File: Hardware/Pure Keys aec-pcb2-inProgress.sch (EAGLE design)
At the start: 56 parts, among them IC1 MCP6004P, IC5 MCP6004P, Q2 20MHz, T1 2N3904, U2 LM4040, U3 328P

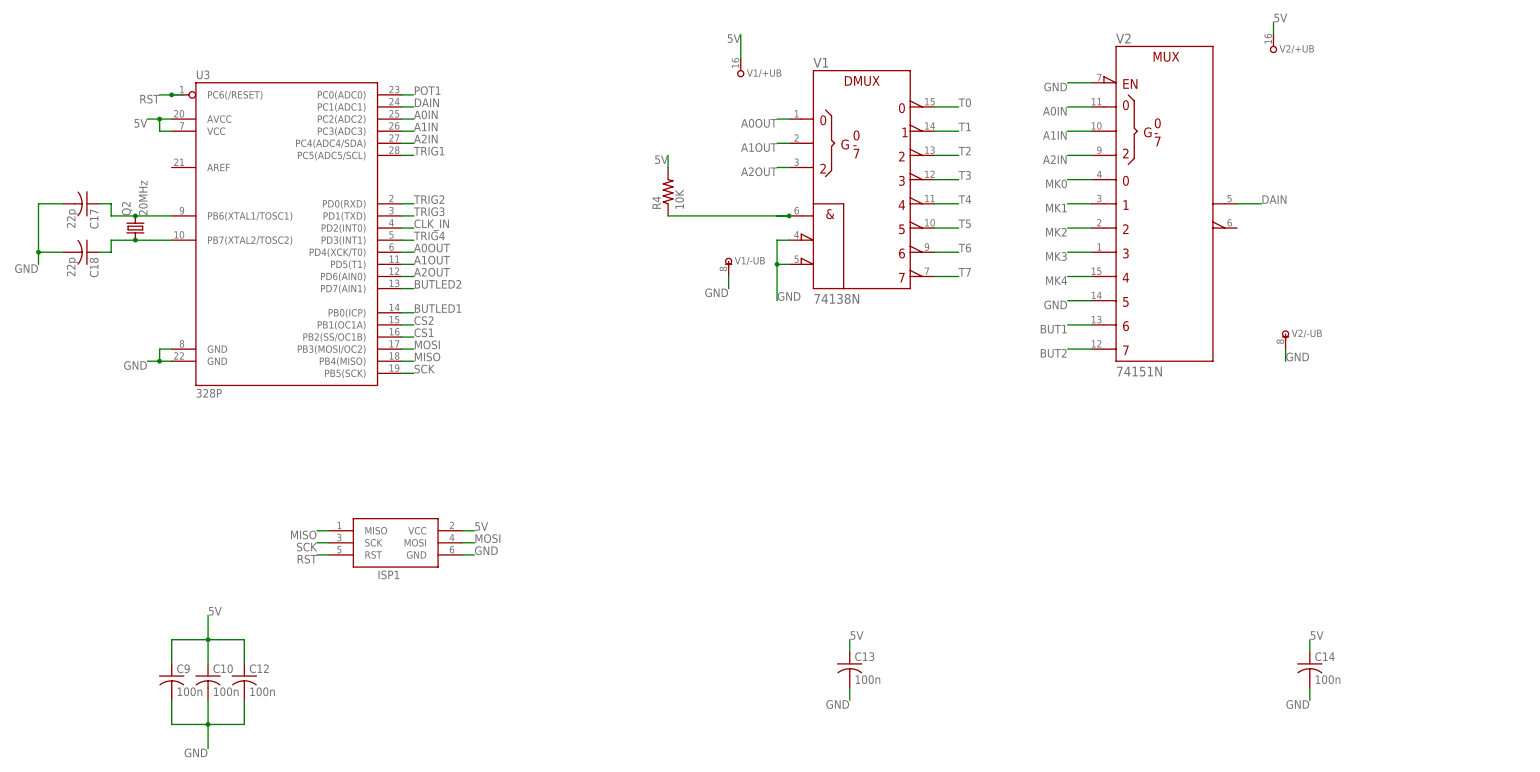
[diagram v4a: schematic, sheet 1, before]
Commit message: Updated routing on in-progress board to make room for 1K pull downs
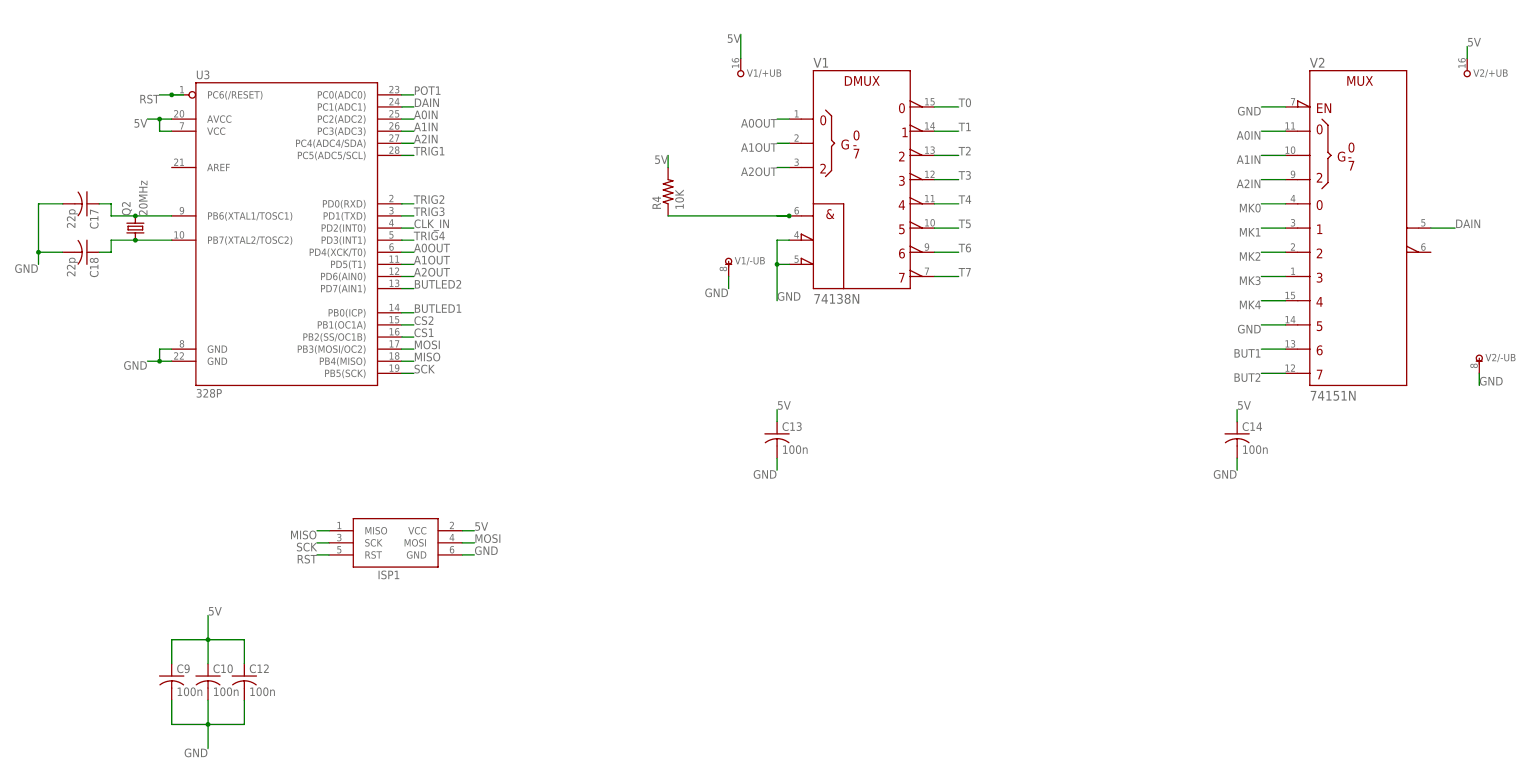
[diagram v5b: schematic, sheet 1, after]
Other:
- moved on the sheet: C13, C14, V2, V2/+UB, V2/-UB
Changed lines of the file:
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@@
 <instance part="C10" gate="G$1" x="25.4" y="43.18"/>
 <instance part="C12" gate="G$1" x="33.02" y="43.18"/>
-<instance part="C13" gate="G$1" x="160.02" y="45.72"/>
-<instance part="C14" gate="G$1" x="256.54" y="45.72"/>
+<instance part="C13" gate="G$1" x="144.78" y="93.98"/>
+<instance part="C14" gate="G$1" x="241.3" y="93.98"/>
 <instance part="V1" gate="1" x="162.56" y="147.32"/>
-<instance part="V2" gate="1" x="226.06" y="142.24"/>
+<instance part="V2" gate="1" x="266.7" y="137.16"/>
 <instance part="U3" gate="G$1" x="40.64" y="139.7"/>
 <instance part="Q2" gate="G$1" x="10.16" y="137.16" rot="R90"/>
@@
 <instance part="V1" gate="/+UB" x="137.16" y="170.18"/>
 <instance part="V1" gate="/-UB" x="134.62" y="129.54"/>
-<instance part="V2" gate="/+UB" x="248.92" y="175.26"/>
-<instance part="V2" gate="/-UB" x="251.46" y="114.3"/>
+<instance part="V2" gate="/+UB" x="289.56" y="170.18"/>
+<instance part="V2" gate="/-UB" x="292.1" y="109.22"/>
 <instance part="R4" gate="G$1" x="121.92" y="144.78" rot="R90"/>
 </instances>
@@
 <segment>
 <pinref part="C14" gate="G$1" pin="2"/>
-<wire x1="256.54" y1="40.64" x2="256.54" y2="38.1" width="0.1524" layer="91"/>
-<label x="256.54" y="38.1" size="1.778" layer="95" rot="R180"/>
+<wire x1="241.3" y1="88.9" x2="241.3" y2="86.36" width="0.1524" layer="91"/>
+<label x="241.3" y="86.36" size="1.778" layer="95" rot="R180"/>
 </segment>
 <segment>
 <pinref part="C13" gate="G$1" pin="2"/>
-<wire x1="160.02" y1="40.64" x2="160.02" y2="38.1" width="0.1524" layer="91"/>
-<label x="160.02" y="38.1" size="1.778" layer="95" rot="R180"/>
+<wire x1="144.78" y1="88.9" x2="144.78" y2="86.36" width="0.1524" layer="91"/>
+<label x="144.78" y="86.36" size="1.778" layer="95" rot="R180"/>
 </segment>
 <segment>
@@
 <segment>
 <pinref part="V2" gate="/-UB" pin="-UB"/>
-<wire x1="251.46" y1="111.76" x2="251.46" y2="109.22" width="0.1524" layer="91"/>
-<label x="251.46" y="109.22" size="1.778" layer="95"/>
+<wire x1="292.1" y1="106.68" x2="292.1" y2="104.14" width="0.1524" layer="91"/>
+<label x="292.1" y="104.14" size="1.778" layer="95"/>
 </segment>
 <segment>
 <pinref part="V2" gate="1" pin="D5"/>
-<wire x1="210.82" y1="121.92" x2="205.74" y2="121.92" width="0.1524" layer="91"/>
-<label x="205.74" y="121.92" size="1.778" layer="95" rot="R180"/>
+<wire x1="251.46" y1="116.84" x2="246.38" y2="116.84" width="0.1524" layer="91"/>
+<label x="246.38" y="116.84" size="1.778" layer="95" rot="R180"/>
 </segment>
 <segment>
 <pinref part="V2" gate="1" pin="!G"/>
-<wire x1="210.82" y1="167.64" x2="205.74" y2="167.64" width="0.1524" layer="91"/>
-<label x="205.74" y="167.64" size="1.778" layer="95" rot="R180"/>
+<wire x1="251.46" y1="162.56" x2="246.38" y2="162.56" width="0.1524" layer="91"/>
+<label x="246.38" y="162.56" size="1.778" layer="95" rot="R180"/>
 </segment>
 </net>
@@
 <segment>
 <pinref part="C13" gate="G$1" pin="1"/>
-<wire x1="160.02" y1="48.26" x2="160.02" y2="50.8" width="0.1524" layer="91"/>
-<label x="160.02" y="50.8" size="1.778" layer="95"/>
+<wire x1="144.78" y1="96.52" x2="144.78" y2="99.06" width="0.1524" layer="91"/>
+<label x="144.78" y="99.06" size="1.778" layer="95"/>
 </segment>
 <segment>
 <pinref part="C14" gate="G$1" pin="1"/>
-<wire x1="256.54" y1="48.26" x2="256.54" y2="50.8" width="0.1524" layer="91"/>
-<label x="256.54" y="50.8" size="1.778" layer="95"/>
+<wire x1="241.3" y1="96.52" x2="241.3" y2="99.06" width="0.1524" layer="91"/>
+<label x="241.3" y="99.06" size="1.778" layer="95"/>
 </segment>
 <segment>
@@
 <segment>
 <pinref part="V2" gate="/+UB" pin="+UB"/>
-<wire x1="248.92" y1="177.8" x2="248.92" y2="180.34" width="0.1524" layer="91"/>
-<label x="248.92" y="180.34" size="1.778" layer="95"/>
+<wire x1="289.56" y1="172.72" x2="289.56" y2="175.26" width="0.1524" layer="91"/>
+<label x="289.56" y="175.26" size="1.778" layer="95"/>
 </segment>
 <segment>
@@
 <segment>
 <pinref part="V2" gate="1" pin="D4"/>
-<wire x1="210.82" y1="127" x2="205.74" y2="127" width="0.1524" layer="91"/>
-<label x="205.74" y="127" size="1.778" layer="95" rot="R180"/>
+<wire x1="251.46" y1="121.92" x2="246.38" y2="121.92" width="0.1524" layer="91"/>
+<label x="246.38" y="121.92" size="1.778" layer="95" rot="R180"/>
 </segment>
 </net>
@@
 <segment>
 <pinref part="V2" gate="1" pin="D3"/>
-<wire x1="210.82" y1="132.08" x2="205.74" y2="132.08" width="0.1524" layer="91"/>
-<label x="205.74" y="132.08" size="1.778" layer="95" rot="R180"/>
+<wire x1="251.46" y1="127" x2="246.38" y2="127" width="0.1524" layer="91"/>
+<label x="246.38" y="127" size="1.778" layer="95" rot="R180"/>
 </segment>
 </net>
@@
 <segment>
 <pinref part="V2" gate="1" pin="D2"/>
-<wire x1="210.82" y1="137.16" x2="205.74" y2="137.16" width="0.1524" layer="91"/>
-<label x="205.74" y="137.16" size="1.778" layer="95" rot="R180"/>
+<wire x1="251.46" y1="132.08" x2="246.38" y2="132.08" width="0.1524" layer="91"/>
+<label x="246.38" y="132.08" size="1.778" layer="95" rot="R180"/>
 </segment>
 </net>
@@
 <segment>
 <pinref part="V2" gate="1" pin="Y"/>
-<wire x1="241.3" y1="142.24" x2="246.38" y2="142.24" width="0.1524" layer="91"/>
-<label x="246.38" y="142.24" size="1.778" layer="95"/>
+<wire x1="281.94" y1="137.16" x2="287.02" y2="137.16" width="0.1524" layer="91"/>
+<label x="287.02" y="137.16" size="1.778" layer="95"/>
 </segment>
 <segment>
@@
 <segment>
 <pinref part="V2" gate="1" pin="D6"/>
-<wire x1="210.82" y1="116.84" x2="205.74" y2="116.84" width="0.1524" layer="91"/>
-<label x="205.74" y="116.84" size="1.778" layer="95" rot="R180"/>
+<wire x1="251.46" y1="111.76" x2="246.38" y2="111.76" width="0.1524" layer="91"/>
+<label x="246.38" y="111.76" size="1.778" layer="95" rot="R180"/>
 </segment>
 </net>
@@
 <segment>
 <pinref part="V2" gate="1" pin="D7"/>
-<wire x1="210.82" y1="111.76" x2="205.74" y2="111.76" width="0.1524" layer="91"/>
-<label x="205.74" y="111.76" size="1.778" layer="95" rot="R180"/>
+<wire x1="251.46" y1="106.68" x2="246.38" y2="106.68" width="0.1524" layer="91"/>
+<label x="246.38" y="106.68" size="1.778" layer="95" rot="R180"/>
 </segment>
 </net>
@@
 <segment>
 <pinref part="V2" gate="1" pin="D1"/>
-<wire x1="210.82" y1="142.24" x2="205.74" y2="142.24" width="0.1524" layer="91"/>
-<label x="205.74" y="142.24" size="1.778" layer="95" rot="R180"/>
+<wire x1="251.46" y1="137.16" x2="246.38" y2="137.16" width="0.1524" layer="91"/>
+<label x="246.38" y="137.16" size="1.778" layer="95" rot="R180"/>
 </segment>
 </net>
@@
 <segment>
 <pinref part="V2" gate="1" pin="D0"/>
-<wire x1="210.82" y1="147.32" x2="205.74" y2="147.32" width="0.1524" layer="91"/>
-<label x="205.74" y="147.32" size="1.778" layer="95" rot="R180"/>
+<wire x1="251.46" y1="142.24" x2="246.38" y2="142.24" width="0.1524" layer="91"/>
+<label x="246.38" y="142.24" size="1.778" layer="95" rot="R180"/>
 </segment>
 </net>
@@
 <segment>
 <pinref part="V2" gate="1" pin="B"/>
-<wire x1="210.82" y1="157.48" x2="205.74" y2="157.48" width="0.1524" layer="91"/>
-<label x="205.74" y="157.48" size="1.778" layer="95" rot="R180"/>
+<wire x1="251.46" y1="152.4" x2="246.38" y2="152.4" width="0.1524" layer="91"/>
+<label x="246.38" y="152.4" size="1.778" layer="95" rot="R180"/>
 </segment>
 <segment>
@@
 <segment>
 <pinref part="V2" gate="1" pin="C"/>
-<wire x1="210.82" y1="152.4" x2="205.74" y2="152.4" width="0.1524" layer="91"/>
-<label x="205.74" y="152.4" size="1.778" layer="95" rot="R180"/>
+<wire x1="251.46" y1="147.32" x2="246.38" y2="147.32" width="0.1524" layer="91"/>
+<label x="246.38" y="147.32" size="1.778" layer="95" rot="R180"/>
 </segment>
 <segment>
@@
 <segment>
 <pinref part="V2" gate="1" pin="A"/>
-<wire x1="210.82" y1="162.56" x2="205.74" y2="162.56" width="0.1524" layer="91"/>
-<label x="205.74" y="162.56" size="1.778" layer="95" rot="R180"/>
-</segment>
-</net>
+<wire x1="251.46" y1="157.48" x2="246.38" y2="157.48" width="0.1524" layer="91"/>
+<label x="246.38" y="157.48" size="1.778" layer="95" rot="R180"/>
+</segment>
+</net>

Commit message: changed in progress board
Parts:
- added R1, R10, R11, R12, R13: 1K, rcl:R-US_R0805
- R3: value 10K -> 2K
- U2: device GMSN:LM4040A50IDBZT -> GMSN-R2Project:LM4040A30IDBZT; MPN (none) -> LM4040A30IDBZT
- V1: value 74138N -> 74238N; device 74ttl-din:74138N -> 74ttl-din:74238N
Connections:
- net GND: now also R1.1, R10.1, R11.1, R12.1, R13.1
- net MK0: now also R1.2
- net MK1: now also R10.2
- net MK2: now also R11.2
- net MK3: now also R12.2
- net MK4: now also R13.2
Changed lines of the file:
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@@
 <part name="CLK_IN" library="GMSN" deviceset="PJ302M" device="" value="PJ302M"/>
 <part name="GND13" library="supply1" library_urn="urn:adsk.eagle:library:371" deviceset="GND" device=""/>
-<part name="U2" library="GMSN" deviceset="LM4040A50IDBZT" device="" value="LM4040"/>
-<part name="R3" library="rcl" deviceset="R-US_" device="R0805" value="10K"/>
-<part name="V1" library="74ttl-din" library_urn="urn:adsk.eagle:library:84" deviceset="74*138" device="N" package3d_urn="urn:adsk.eagle:package:1462/1"/>
+<part name="U2" library="GMSN-R2Project" deviceset="LM4040A30IDBZT" device="" value="LM4040">
+<attribute name="MPN" value="LM4040A30IDBZT"/>
+</part>
+<part name="R3" library="rcl" deviceset="R-US_" device="R0805" value="2K"/>
+<part name="V1" library="74ttl-din" library_urn="urn:adsk.eagle:library:84" deviceset="74*238" device="N" package3d_urn="urn:adsk.eagle:package:1462/1"/>
 <part name="V2" library="74ttl-din" library_urn="urn:adsk.eagle:library:84" deviceset="74*151" device="N" package3d_urn="urn:adsk.eagle:package:1462/1"/>
 <part name="U3" library="SparkFun-IC-Microcontroller" deviceset="ATMEGA328P_PDIP" device="" value="328P"/>
@@
 <part name="R8" library="rcl" deviceset="R-US_" device="R0805" value="100K"/>
 <part name="R9" library="rcl" deviceset="R-US_" device="R0805" value="100K"/>
+<part name="R1" library="rcl" deviceset="R-US_" device="R0805" value="1K"/>
+<part name="R10" library="rcl" deviceset="R-US_" device="R0805" value="1K"/>
+<part name="R11" library="rcl" deviceset="R-US_" device="R0805" value="1K"/>
+<part name="R12" library="rcl" deviceset="R-US_" device="R0805" value="1K"/>
+<part name="R13" library="rcl" deviceset="R-US_" device="R0805" value="1K"/>
 </parts>
 <sheets>
@@
 <instance part="V2" gate="/-UB" x="292.1" y="109.22"/>
 <instance part="R4" gate="G$1" x="121.92" y="144.78" rot="R90"/>
+<instance part="R1" gate="G$1" x="198.12" y="137.16" rot="R90"/>
+<instance part="R10" gate="G$1" x="205.74" y="132.08" rot="R90"/>
+<instance part="R11" gate="G$1" x="215.9" y="127" rot="R90"/>
+<instance part="R12" gate="G$1" x="223.52" y="121.92" rot="R90"/>
+<instance part="R13" gate="G$1" x="233.68" y="116.84" rot="R90"/>
 </instances>
 <busses>
@@
 <label x="246.38" y="162.56" size="1.778" layer="95" rot="R180"/>
 </segment>
+<segment>
+<pinref part="R1" gate="G$1" pin="1"/>
+<wire x1="198.12" y1="132.08" x2="198.12" y2="129.54" width="0.1524" layer="91"/>
+<label x="198.12" y="129.54" size="1.778" layer="95"/>
+</segment>
+<segment>
+<pinref part="R10" gate="G$1" pin="1"/>
+<wire x1="205.74" y1="127" x2="205.74" y2="124.46" width="0.1524" layer="91"/>
+<label x="205.74" y="124.46" size="1.778" layer="95"/>
+</segment>
+<segment>
+<pinref part="R11" gate="G$1" pin="1"/>
+<wire x1="215.9" y1="121.92" x2="215.9" y2="119.38" width="0.1524" layer="91"/>
+<label x="215.9" y="119.38" size="1.778" layer="95"/>
+</segment>
+<segment>
+<pinref part="R12" gate="G$1" pin="1"/>
+<wire x1="223.52" y1="116.84" x2="223.52" y2="114.3" width="0.1524" layer="91"/>
+<label x="223.52" y="114.3" size="1.778" layer="95"/>
+</segment>
+<segment>
+<pinref part="R13" gate="G$1" pin="1"/>
+<wire x1="233.68" y1="111.76" x2="233.68" y2="109.22" width="0.1524" layer="91"/>
+<label x="233.68" y="109.22" size="1.778" layer="95"/>
+</segment>
 </net>
 <net name="RST" class="0">
@@
 <segment>
 <pinref part="V2" gate="1" pin="D4"/>
-<wire x1="251.46" y1="121.92" x2="246.38" y2="121.92" width="0.1524" layer="91"/>
+<wire x1="251.46" y1="121.92" x2="248.92" y2="121.92" width="0.1524" layer="91"/>
 <label x="246.38" y="121.92" size="1.778" layer="95" rot="R180"/>
+<pinref part="R13" gate="G$1" pin="2"/>
+<wire x1="248.92" y1="121.92" x2="246.38" y2="121.92" width="0.1524" layer="91"/>
+<wire x1="233.68" y1="121.92" x2="246.38" y2="121.92" width="0.1524" layer="91"/>
 </segment>
 </net>
@@
 <segment>
 <pinref part="V2" gate="1" pin="D3"/>
-<wire x1="251.46" y1="127" x2="246.38" y2="127" width="0.1524" layer="91"/>
 <label x="246.38" y="127" size="1.778" layer="95" rot="R180"/>
+<pinref part="R12" gate="G$1" pin="2"/>
+<wire x1="223.52" y1="127" x2="251.46" y2="127" width="0.1524" layer="91"/>
 </segment>
 </net>
@@
 <segment>
 <pinref part="V2" gate="1" pin="D2"/>
-<wire x1="251.46" y1="132.08" x2="246.38" y2="132.08" width="0.1524" layer="91"/>
 <label x="246.38" y="132.08" size="1.778" layer="95" rot="R180"/>
+<pinref part="R11" gate="G$1" pin="2"/>
+<wire x1="215.9" y1="132.08" x2="251.46" y2="132.08" width="0.1524" layer="91"/>
 </segment>
 </net>
@@
 <segment>
 <pinref part="V2" gate="1" pin="D1"/>
-<wire x1="251.46" y1="137.16" x2="246.38" y2="137.16" width="0.1524" layer="91"/>
 <label x="246.38" y="137.16" size="1.778" layer="95" rot="R180"/>
+<pinref part="R10" gate="G$1" pin="2"/>
+<wire x1="205.74" y1="137.16" x2="251.46" y2="137.16" width="0.1524" layer="91"/>
 </segment>
 </net>
@@
 <segment>
 <pinref part="V2" gate="1" pin="D0"/>
-<wire x1="251.46" y1="142.24" x2="246.38" y2="142.24" width="0.1524" layer="91"/>
 <label x="246.38" y="142.24" size="1.778" layer="95" rot="R180"/>
-</segment>
-</net>
+<pinref part="R1" gate="G$1" pin="2"/>
+<wire x1="251.46" y1="142.24" x2="198.12" y2="142.24" width="0.1524" layer="91"/>
+</segment>
+</net>
